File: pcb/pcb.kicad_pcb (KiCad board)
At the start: 2 copper layers, 33 parts, among them J1 NMJ4HCD2, J2 NMJ4HCD2, U1 RC4558

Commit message: add 3pdt footprint and symbol
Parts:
- added SW1: ~, 3PDT:SW_3PDT_GENERIC, F.Cu at (247.7, 81.3)
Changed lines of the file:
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@@
 	(net 21 "unconnected-(RV2-Pad3)")
 	(net 22 "/VCC")
+	(net 23 "unconnected-(SW1-Pad5)")
+	(net 24 "unconnected-(SW1-Pad1)")
+	(net 25 "unconnected-(SW1-Pad9)")
+	(net 26 "unconnected-(SW1-Pad8)")
+	(net 27 "unconnected-(SW1-Pad2)")
+	(net 28 "unconnected-(SW1-Pad7)")
+	(net 29 "unconnected-(SW1-Pad6)")
+	(net 30 "unconnected-(SW1-Pad3)")
+	(net 31 "unconnected-(SW1-Pad4)")
 	(footprint "Resistor_THT:R_Axial_DIN0207_L6.3mm_D2.5mm_P10.16mm_Horizontal"
 		(layer "F.Cu")
@@
 		)
 	)
+	(footprint "3PDT:SW_3PDT_GENERIC"
+		(layer "F.Cu")
+		(at 247.7 81.3)
+		(property "Reference" "SW1"
+			(at 0 -14.5 0)
+			(unlocked yes)
+			(layer "F.SilkS")
+			(effects
+				(font
+					(size 1 1)
+					(thickness 0.1)
+				)
+			)
+		)
+		(property "Value" "~"
+			(at 0 -13 0)
+			(unlocked yes)
+			(layer "F.Fab")
+			(effects
+				(font
+					(size 1 1)
+					(thickness 0.15)
+				)
+			)
+		)
+		(property "Datasheet" ""
+			(at 0 0 0)
+			(unlocked yes)
+			(layer "F.Fab")
+			(hide yes)
+			(effects
+				(font
+					(size 1 1)
+					(thickness 0.15)
+				)
+			)
+		)
+		(property "Description" ""
+			(at 0 0 0)
+			(unlocked yes)
+			(layer "F.Fab")
+			(hide yes)
+			(effects
+				(font
+					(size 1 1)
+					(thickness 0.15)
+				)
+			)
+		)
+		(sheetname "/")
+		(sheetfile "pcb.kicad_sch")
+		(attr smd)
+		(fp_text user "${REFERENCE}"
+			(at 0 -11.5 0)
+			(unlocked yes)
+			(layer "F.Fab")
+			(effects
+				(font
+					(size 1 1)
+					(thickness 0.15)
+				)
+			)
+		)
+		(pad "1" thru_hole roundrect
+			(at 5.3 -4.7)
+			(size 2.75 1.45)
+			(drill oval 2.25 1.1)
+			(layers "*.Cu" "*.Mask")
+			(remove_unused_layers no)
+			(roundrect_rratio 0.1968503937)
+			(net 24 "unconnected-(SW1-Pad1)")
+			(pinfunction "1")
+			(pintype "bidirectional")
+		)
+		(pad "2" thru_hole roundrect
+			(at 0 -4.7)
+			(size 2.75 1.45)
+			(drill oval 2.25 1.1)
+			(layers "*.Cu" "*.Mask")
+			(remove_unused_layers no)
+			(roundrect_rratio 0.1968503937)
+			(net 27 "unconnected-(SW1-Pad2)")
+			(pinfunction "2")
+			(pintype "bidirectional")
+		)
+		(pad "3" thru_hole roundrect
+			(at -5.3 -4.7)
+			(size 2.75 1.45)
+			(drill oval 2.25 1.1)
+			(layers "*.Cu" "*.Mask")
+			(remove_unused_layers no)
+			(roundrect_rratio 0.1968503937)
+			(net 30 "unconnected-(SW1-Pad3)")
+			(pinfunction "3")
+			(pintype "bidirectional")
+		)
+		(pad "4" thru_hole roundrect
+			(at 5.3 0)
+			(size 2.75 1.45)
+			(drill oval 2.25 1.1)
+			(layers "*.Cu" "*.Mask")
+			(remove_unused_layers no)
+			(roundrect_rratio 0.1968503937)
+			(net 31 "unconnected-(SW1-Pad4)")
+			(pinfunction "4")
+			(pintype "bidirectional")
+		)
+		(pad "5" thru_hole roundrect
+			(at 0 0)
+			(size 2.75 1.45)
+			(drill oval 2.25 1.1)
+			(layers "*.Cu" "*.Mask")
+			(remove_unused_layers no)
+			(roundrect_rratio 0.1968503937)
+			(net 23 "unconnected-(SW1-Pad5)")
+			(pinfunction "5")
+			(pintype "bidirectional")
+		)
+		(pad "6" thru_hole roundrect
+			(at -5.3 0)
+			(size 2.75 1.45)
+			(drill oval 2.25 1.1)
+			(layers "*.Cu" "*.Mask")
+			(remove_unused_layers no)
+			(roundrect_rratio 0.1968503937)
+			(net 29 "unconnected-(SW1-Pad6)")
+			(pinfunction "6")
+			(pintype "bidirectional")
+		)
+		(pad "7" thru_hole roundrect
+			(at 5.3 4.7)
+			(size 2.75 1.45)
+			(drill oval 2.25 1.1)
+			(layers "*.Cu" "*.Mask")
+			(remove_unused_layers no)
+			(roundrect_rratio 0.1968503937)
+			(net 28 "unconnected-(SW1-Pad7)")
+			(pinfunction "7")
+			(pintype "bidirectional")
+		)
+		(pad "8" thru_hole roundrect
+			(at 0 4.7)
+			(size 2.75 1.45)
+			(drill oval 2.25 1.1)
+			(layers "*.Cu" "*.Mask")
+			(remove_unused_layers no)
+			(roundrect_rratio 0.1968503937)
+			(net 26 "unconnected-(SW1-Pad8)")
+			(pinfunction "8")
+			(pintype "bidirectional")
+		)
+		(pad "9" thru_hole roundrect
+			(at -5.3 4.7)
+			(size 2.75 1.45)
+			(drill oval 2.25 1.1)
+			(layers "*.Cu" "*.Mask")
+			(remove_unused_layers no)
+			(roundrect_rratio 0.1968503937)
+			(net 25 "unconnected-(SW1-Pad9)")
+			(pinfunction "9")
+			(pintype "bidirectional")
+		)
+		(embedded_fonts no)
+	)
 	(footprint "Capacitor_THT:C_Rect_L7.2mm_W2.5mm_P5.00mm"

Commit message: FIX LIBRARIES :O
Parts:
- SW1: value ~ -> FSWITCH
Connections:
- SW1 pad 1: unconnected-(SW1-Pad1) -> GND
- SW1 pad 2: unconnected-(SW1-Pad2) -> GND
- SW1 pad 5: unconnected-(SW1-Pad5) -> GND
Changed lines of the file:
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@@
 	(net 21 "unconnected-(RV2-Pad3)")
 	(net 22 "/VCC")
-	(net 23 "unconnected-(SW1-Pad5)")
-	(net 24 "unconnected-(SW1-Pad1)")
-	(net 25 "unconnected-(SW1-Pad9)")
-	(net 26 "unconnected-(SW1-Pad8)")
-	(net 27 "unconnected-(SW1-Pad2)")
-	(net 28 "unconnected-(SW1-Pad7)")
-	(net 29 "unconnected-(SW1-Pad6)")
-	(net 30 "unconnected-(SW1-Pad3)")
-	(net 31 "unconnected-(SW1-Pad4)")
+	(net 23 "unconnected-(SW1-Pad9)")
+	(net 24 "unconnected-(SW1-Pad8)")
+	(net 25 "unconnected-(SW1-Pad7)")
+	(net 26 "unconnected-(SW1-Pad6)")
+	(net 27 "unconnected-(SW1-Pad3)")
+	(net 28 "unconnected-(SW1-Pad4)")
 	(footprint "Resistor_THT:R_Axial_DIN0207_L6.3mm_D2.5mm_P10.16mm_Horizontal"
 		(layer "F.Cu")
@@
 			)
 		)
-		(property "Value" "~"
+		(property "Value" "FSWITCH"
 			(at 0 -13 0)
 			(unlocked yes)
@@
 			(remove_unused_layers no)
 			(roundrect_rratio 0.1968503937)
-			(net 24 "unconnected-(SW1-Pad1)")
+			(net 1 "GND")
 			(pinfunction "1")
 			(pintype "bidirectional")
@@
 			(remove_unused_layers no)
 			(roundrect_rratio 0.1968503937)
-			(net 27 "unconnected-(SW1-Pad2)")
+			(net 1 "GND")
 			(pinfunction "2")
 			(pintype "bidirectional")
@@
 			(remove_unused_layers no)
 			(roundrect_rratio 0.1968503937)
-			(net 30 "unconnected-(SW1-Pad3)")
+			(net 27 "unconnected-(SW1-Pad3)")
 			(pinfunction "3")
 			(pintype "bidirectional")
@@
 			(remove_unused_layers no)
 			(roundrect_rratio 0.1968503937)
-			(net 31 "unconnected-(SW1-Pad4)")
+			(net 28 "unconnected-(SW1-Pad4)")
 			(pinfunction "4")
 			(pintype "bidirectional")
@@
 			(remove_unused_layers no)
 			(roundrect_rratio 0.1968503937)
-			(net 23 "unconnected-(SW1-Pad5)")
+			(net 1 "GND")
 			(pinfunction "5")
 			(pintype "bidirectional")
@@
 			(remove_unused_layers no)
 			(roundrect_rratio 0.1968503937)
-			(net 29 "unconnected-(SW1-Pad6)")
+			(net 26 "unconnected-(SW1-Pad6)")
 			(pinfunction "6")
 			(pintype "bidirectional")
@@
 			(remove_unused_layers no)
 			(roundrect_rratio 0.1968503937)
-			(net 28 "unconnected-(SW1-Pad7)")
+			(net 25 "unconnected-(SW1-Pad7)")
 			(pinfunction "7")
 			(pintype "bidirectional")
@@
 			(remove_unused_layers no)
 			(roundrect_rratio 0.1968503937)
-			(net 26 "unconnected-(SW1-Pad8)")
+			(net 24 "unconnected-(SW1-Pad8)")
 			(pinfunction "8")
 			(pintype "bidirectional")
@@
 			(remove_unused_layers no)
 			(roundrect_rratio 0.1968503937)
-			(net 25 "unconnected-(SW1-Pad9)")
+			(net 23 "unconnected-(SW1-Pad9)")
 			(pinfunction "9")
 			(pintype "bidirectional")

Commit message: Finalize pcb
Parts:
- added C14: 100n, Capacitor_THT:C_Rect_L7.2mm_W2.5mm_P5.00mm, F.Cu at (159.5, 85.0)
- added D5: LED, LED_THT:LED_D3.0mm, F.Cu at (150.0, 100.5)
- added R12: 1k, Resistor_THT:R_Axial_DIN0207_L6.3mm_D2.5mm_P10.16mm_Horizontal, F.Cu at (133.0, 59.4)
- added R13: 1k, Resistor_THT:R_Axial_DIN0207_L6.3mm_D2.5mm_P10.16mm_Horizontal, F.Cu at (163.7, 62.0)
- added R14: 1k, Resistor_THT:R_Axial_DIN0207_L6.3mm_D2.5mm_P10.16mm_Horizontal, F.Cu at (174.0, 69.5)
- added R7: 1k, Resistor_THT:R_Axial_DIN0207_L6.3mm_D2.5mm_P10.16mm_Horizontal, F.Cu at (145.0, 106.0)
- SW1: footprint 3PDT:SW_3PDT_GENERIC -> 3PDT:3PDT
- moved SW1 104.6 mm to (150.0, 118.7)
- moved R10 99.6 mm to (137.0, 62.5)
- moved RV3 99.5 mm to (179.0, 56.4), turned to 90 degrees
- moved C10 96.2 mm to (147.0, 69.5), turned to 90 degrees
- moved D2 95.0 mm to (153.5, 67.5)
- moved R9 93.9 mm to (118.4, 65.0)
- moved R8 93.8 mm to (118.5, 61.0)
- moved C8 91.7 mm to (134.5, 74.5)
- moved RV1 91.2 mm to (131.0, 56.4), turned to 90 degrees
- moved RV2 88.5 mm to (155.0, 56.4), turned to 90 degrees
- moved C11 87.9 mm to (167.0, 63.0), turned to -90 degrees
- moved D4 86.4 mm to (150.5, 72.0), turned to 90 degrees
- moved D3 82.5 mm to (153.8, 72.0)
- moved C9 80.6 mm to (142.5, 71.0), turned to 90 degrees
- moved R11 76.8 mm to (144.9, 95.0)
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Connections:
- C4 pad 1: /VIN -> /VAMPIN
- R4 pad 1: /VIN -> /VAMPIN
- RV1 pad 1: /AMP1- -> unconnected-(RV1-Pad1)
- RV1 pad 2: /AMP1OUT -> Net-(R12-Pad1)
- RV1 pad 3: unconnected-(RV1-Pad3) -> /AMP1-
- RV2 pad 1: /VCLIP -> unconnected-(RV2-Pad1)
- RV2 pad 3: unconnected-(RV2-Pad3) -> Net-(R13-Pad2)
- RV3 pad 1: GND -> Net-(R14-Pad2)
- RV3 pad 2: /VOUT -> /VVOLOUT
- RV3 pad 3: Net-(C13-Pad2) -> GND
- SW1 pad 1: GND -> /VAMPIN
- SW1 pad 2: GND -> /VIN
- SW1 pad 3: unconnected-(SW1-Pad3) -> Net-(SW1-Pad3)
- SW1 pad 4: unconnected-(SW1-Pad4) -> /VCC
- SW1 pad 5: GND -> Net-(R7-Pad2)
- SW1 pad 6: unconnected-(SW1-Pad6) -> GND
- SW1 pad 7: unconnected-(SW1-Pad7) -> /VVOLOUT
- SW1 pad 8: unconnected-(SW1-Pad8) -> /VOUT
- SW1 pad 9: unconnected-(SW1-Pad9) -> Net-(SW1-Pad3)
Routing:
- net /VCC: track 0.00 -> 75.6 mm
- net /VVOLOUT: track 0.00 -> 74.1 mm
- net GND: track 0.00 -> 63.1 mm
- net /AMP2+: track 0.00 -> 43.6 mm
- net /VBIAS: track 0.00 -> 41.1 mm
- net /AMP1-: track 0.00 -> 39.6 mm
- net /AMP2-: track 0.00 -> 36.5 mm
- net /AMP1+: track 0.00 -> 34.2 mm
- net Net-(C11-Pad1): track 0.00 -> 27.6 mm
- net /VCLIP: track 0.00 -> 27.5 mm
- net /AMP1OUT: track 0.00 -> 21.8 mm
- net Net-(C4-Pad2): track 0.00 -> 17.9 mm
- net Net-(R7-Pad2): track 0.00 -> 17.9 mm
- net /VOUT: track 0.00 -> 17.8 mm
- net /VIN: track 0.00 -> 17.3 mm
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- added copper zone on B.Cu, net GND
- added copper zone on F.Cu, net GND
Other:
- board outline added: 69 x 97.5 mm

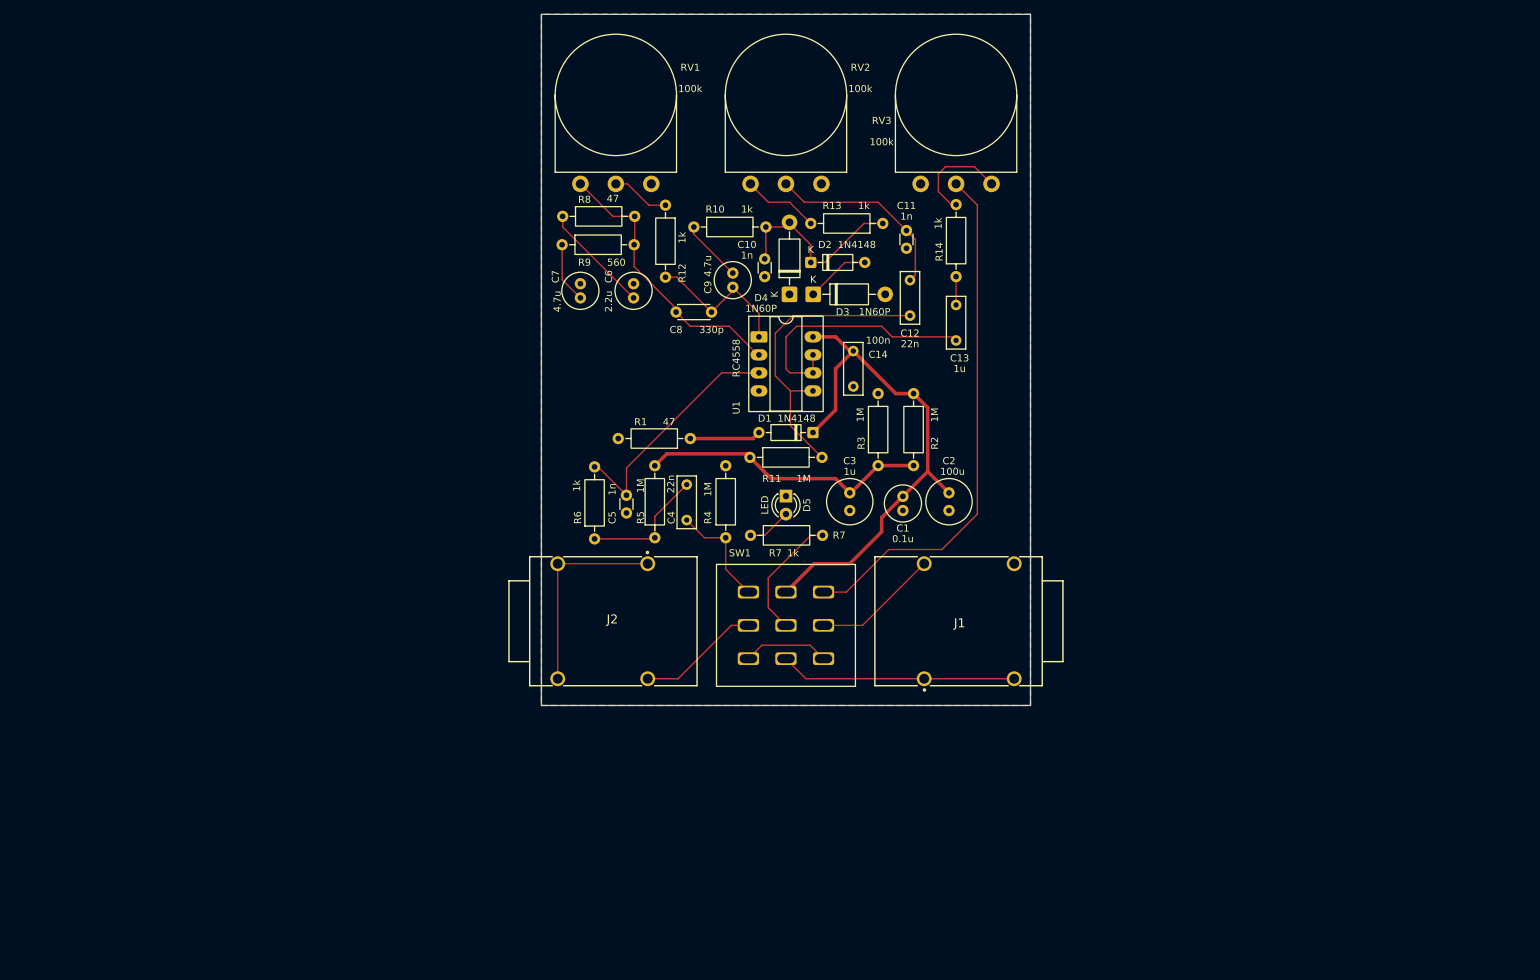
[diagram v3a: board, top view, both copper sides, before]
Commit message: Rework Amplifier Stage
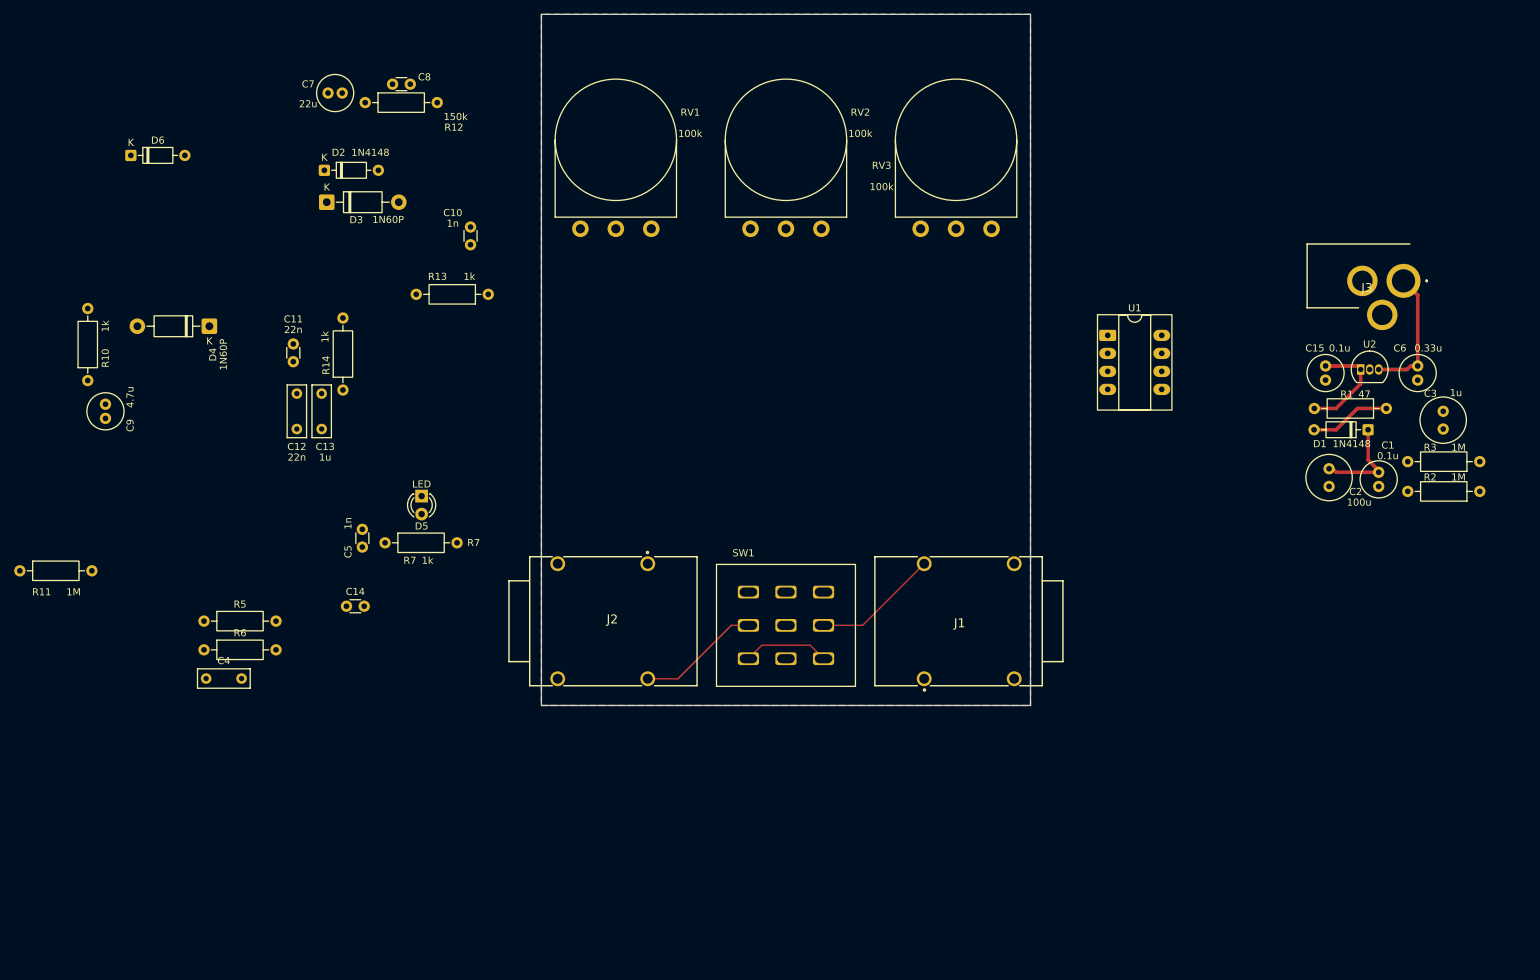
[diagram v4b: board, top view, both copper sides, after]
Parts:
- removed R4: 1M, Resistor_THT:R_Axial_DIN0207_L6.3mm_D2.5mm_P10.16mm_Horizontal
- removed R8: 47, Resistor_THT:R_Axial_DIN0207_L6.3mm_D2.5mm_P10.16mm_Horizontal
- removed R9: 560, Resistor_THT:R_Axial_DIN0207_L6.3mm_D2.5mm_P10.16mm_Horizontal
- added C15: 0.1u, Capacitor_THT:C_Radial_D5.0mm_H11.0mm_P2.00mm, F.Cu at (226.1, 82.1)
- added D6: 1N4148, Diode_THT:D_DO-35_SOD27_P7.62mm_Horizontal, F.Cu at (57.6, 52.4)
- added J3: 694106301002, PowerJackFemale:694106301002, F.Cu at (237.1, 70.1)
- added U2: L78L09_TO92, Package_TO_SOT_THT:TO-92_Inline, F.Cu at (231.1, 82.6)
- C11: value 1n -> 22n
- C14: footprint Capacitor_THT:C_Rect_L7.2mm_W2.5mm_P5.00mm -> Capacitor_THT:C_Disc_D3.0mm_W1.6mm_P2.50mm
- C6: value 2.2u -> 0.33u
- C7: value 4.7u -> 22u
- C8: value 330p -> 150p; footprint Capacitor_THT:C_Disc_D4.3mm_W1.9mm_P5.00mm -> Capacitor_THT:C_Disc_D3.0mm_W1.6mm_P2.50mm
- R12: value 1k -> 150k
- moved C6 111.2 mm to (239.1, 82.1)
- moved R11 104.2 mm to (41.9, 111.0)
- moved R1 98.3 mm to (234.7, 88.1)
- moved C9 90.4 mm to (54.0, 89.5)
- moved C13 90.4 mm to (84.5, 91.0)
- moved R10 88.2 mm to (51.5, 84.2), turned to 90 degrees
- moved C11 88.0 mm to (80.5, 79.0)
- moved C12 88.0 mm to (81.0, 86.0)
- moved R14 88.0 mm to (87.5, 85.5)
- moved R3 84.9 mm to (247.9, 95.6), turned to 180 degrees
- moved C3 84.2 mm to (242.7, 91.0), turned to 90 degrees
- moved D4 82.0 mm to (68.7, 76.5), turned to 180 degrees
- moved R2 81.1 mm to (247.9, 99.8), turned to 180 degrees
- moved D1 78.3 mm to (232.1, 91.1)
- moved C14 77.9 mm to (88.0, 116.0), turned to 0 degrees
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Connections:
- C5 pad 2: /AMP1+ -> /VAMPIN
- C6 pad 1: GND -> /VCCRAW
- C6 pad 2: Net-(C6-Pad2) -> GND
- C7 pad 1: GND -> Net-(C7-Pad1)
- C7 pad 2: Net-(C7-Pad2) -> /AMP1-
- D4 pad 2: /VCLIP -> Net-(D4-A)
- R1 pad 2: +9V -> /V9
- R12 pad 1: Net-(R12-Pad1) -> /AMP1-
- RV1 pad 2: Net-(R12-Pad1) -> Net-(C7-Pad1)
- RV1 pad 3: /AMP1- -> GND
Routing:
- net /VVOLOUT: track 74.1 -> 0.00 mm
- net GND: track 63.1 -> 0.00 mm
- net /VCC: track 75.6 -> 13.8 mm
- net /AMP2+: track 43.6 -> 0.00 mm
- net /VBIAS: track 41.1 -> 0.00 mm
- net /AMP1-: track 39.6 -> 0.00 mm
- net /AMP2-: track 36.5 -> 0.00 mm
- net /AMP1+: track 34.2 -> 0.00 mm
- net Net-(C11-Pad1): track 27.6 -> 0.00 mm
- net /VCLIP: track 27.5 -> 0.00 mm
- net /AMP1OUT: track 21.8 -> 0.00 mm
- net /VCCRAW: track 0.00 -> 18.5 mm
- net Net-(C4-Pad2): track 17.9 -> 0.00 mm
- net Net-(R7-Pad2): track 17.9 -> 0.00 mm
- net Net-(C6-Pad2): track 15.6 -> 0.00 mm
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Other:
- board text added: "RV1"

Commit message: Finalize pcb
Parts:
- added REF**: MountingHole_3.2mm_M3, MountingHole:MountingHole_3.2mm_M3, F.Cu at (196.0, 133.5)
- added REF**: MountingHole_3.2mm_M3, MountingHole:MountingHole_3.2mm_M3, F.Cu at (104.0, 133.5)
- added REF**: MountingHole_3.2mm_M3, MountingHole:MountingHole_3.2mm_M3, F.Cu at (196.0, 41.5)
- added REF**: MountingHole_3.2mm_M3, MountingHole:MountingHole_3.2mm_M3, F.Cu at (104.0, 41.5)
- moved R11 117.7 mm to (158.4, 94.0), turned to 90 degrees
- moved R2 86.1 mm to (163.3, 83.8), turned to -90 degrees
- moved C14 82.7 mm to (161.9, 79.0), turned to 180 degrees
- moved C3 82.5 mm to (160.5, 98.0), turned to -90 degrees
- moved D6 82.0 mm to (133.3, 83.9), turned to 90 degrees
- moved R5 80.7 mm to (144.9, 94.0)
- moved R3 80.6 mm to (167.3, 93.3), turned to -90 degrees
- moved C13 76.5 mm to (159.5, 75.8), turned to 0 degrees
- moved C9 76.1 mm to (130.0, 94.2), turned to -90 degrees
- moved R14 75.7 mm to (162.0, 71.9)
- moved R6 74.7 mm to (140.4, 104.2), turned to 90 degrees
- moved R10 72.1 mm to (121.6, 101.1)
- moved C4 70.1 mm to (135.2, 105.6), turned to 90 degrees
- moved C11 69.0 mm to (148.8, 68.6), turned to 0 degrees
- moved C12 67.7 mm to (147.5, 73.2), turned to 0 degrees
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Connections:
- RV1 pad 1: unconnected-(RV1-Pad1) -> GND
- RV1 pad 3: GND -> unconnected-(RV1-Pad3)
- RV3 pad 1: Net-(R14-Pad2) -> GND
- RV3 pad 3: GND -> Net-(R14-Pad2)
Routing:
- net /VVOLOUT: track 0.00 -> 81.2 mm
- net /VCC: track 13.8 -> 79.7 mm
- net /VCLIP: track 0.00 -> 45.6 mm
- net /AMP1OUT: track 0.00 -> 25.7 mm
- net /AMP1-: track 0.00 -> 25.6 mm
- net /AMP2+: track 0.00 -> 25.4 mm
- net Net-(C7-Pad1): track 0.00 -> 19.5 mm
- net Net-(R7-Pad2): track 0.00 -> 19.4 mm
- net Net-(C4-Pad2): track 0.00 -> 18.8 mm
- net /VAMPIN: track 0.00 -> 18.6 mm
- net /AMP2-: track 0.00 -> 17.7 mm
- net /VBIAS: track 0.00 -> 17.4 mm
- net Net-(D2-A): track 0.00 -> 10.9 mm
- net /AMP1+: track 0.00 -> 10.8 mm
- net Net-(D4-A): track 0.00 -> 10.7 mm
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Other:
- board size 69 x 97.5 mm -> 100 x 100 mm

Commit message: 1590b pcb
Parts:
- removed REF** (x4): MountingHole_3.2mm_M3, MountingHole:MountingHole_3.2mm_M3
- J1, J2: footprint NMJ4HCD2:NMJ4HCD2 -> Connector_PinHeader_2.00mm:PinHeader_1x04_P2.00mm_Vertical
- J3: footprint PowerJackFemale:694106301002 -> Connector_PinHeader_2.00mm:PinHeader_1x03_P2.00mm_Vertical
- RV1, RV2, RV3: footprint Potentiometer_THT:Potentiometer_Omeg_PC16BU_Vertical -> Connector_PinHeader_2.00mm:PinHeader_1x03_P2.00mm_Vertical
- U2: value L78L09_TO92 -> L78L09
- moved RV1 77.9 mm to (161.7, 135.5), turned to 180 degrees
- moved RV3 64.2 mm to (184.0, 128.0), turned to 180 degrees
- moved R13 60.8 mm to (189.5, 90.8), turned to -90 degrees
- moved R14 59.9 mm to (189.0, 125.4), turned to -90 degrees
- moved C10 57.8 mm to (177.0, 95.0), turned to 180 degrees
- moved RV2 56.3 mm to (189.5, 108.5), turned to 180 degrees
- moved C7 56.1 mm to (161.0, 126.0), turned to 90 degrees
- moved J2 55.4 mm to (161.7, 146.0)
- moved D6 49.7 mm to (182.5, 91.0)
- moved C12 49.5 mm to (184.5, 106.1), turned to -90 degrees
- moved D4 48.7 mm to (177.5, 91.0)
- moved D3 48.5 mm to (172.5, 80.8)
- moved D2 48.1 mm to (167.5, 83.4)
- moved C11 48.0 mm to (183.8, 101.5)
- moved C13 46.2 mm to (184.0, 115.0), turned to -90 degrees
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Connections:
- RV1 pad 3: unconnected-(RV1-Pad3) -> GND
- RV2 pad 1: unconnected-(RV2-Pad1) -> GND
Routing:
- net /VVOLOUT: track 81.2 -> 10.8 mm
- net /VBIAS: track 17.4 -> 68.1 mm
- net /AMP2+: track 25.4 -> 11.4 mm
- net Net-(C4-Pad2): track 18.8 -> 6.87 mm
- net Net-(C7-Pad1): track 19.5 -> 9.28 mm
- net /VOUT: track 17.8 -> 8.00 mm
- net /VIN: track 17.3 -> 8.00 mm
- net Net-(C9-Pad2): track 10.4 -> 4.25 mm
- net Net-(D1-A): track 12.0 -> 5.99 mm
- net Net-(R14-Pad2): track 7.92 -> 13.7 mm
- net /V9: track 16.4 -> 10.7 mm
- net /AMP1-: track 25.6 -> 31.0 mm
- net /AMP1+: track 10.8 -> 5.78 mm
- net /AMP1OUT: track 25.7 -> 20.8 mm
- net /VAMPIN: track 18.6 -> 13.9 mm
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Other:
- board size 100 x 100 mm -> 35 x 88 mm
- board text removed: "RV1"
